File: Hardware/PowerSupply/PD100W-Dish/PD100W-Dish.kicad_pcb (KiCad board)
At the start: 4 copper layers, 66.8 x 66.2 mm, 164 parts

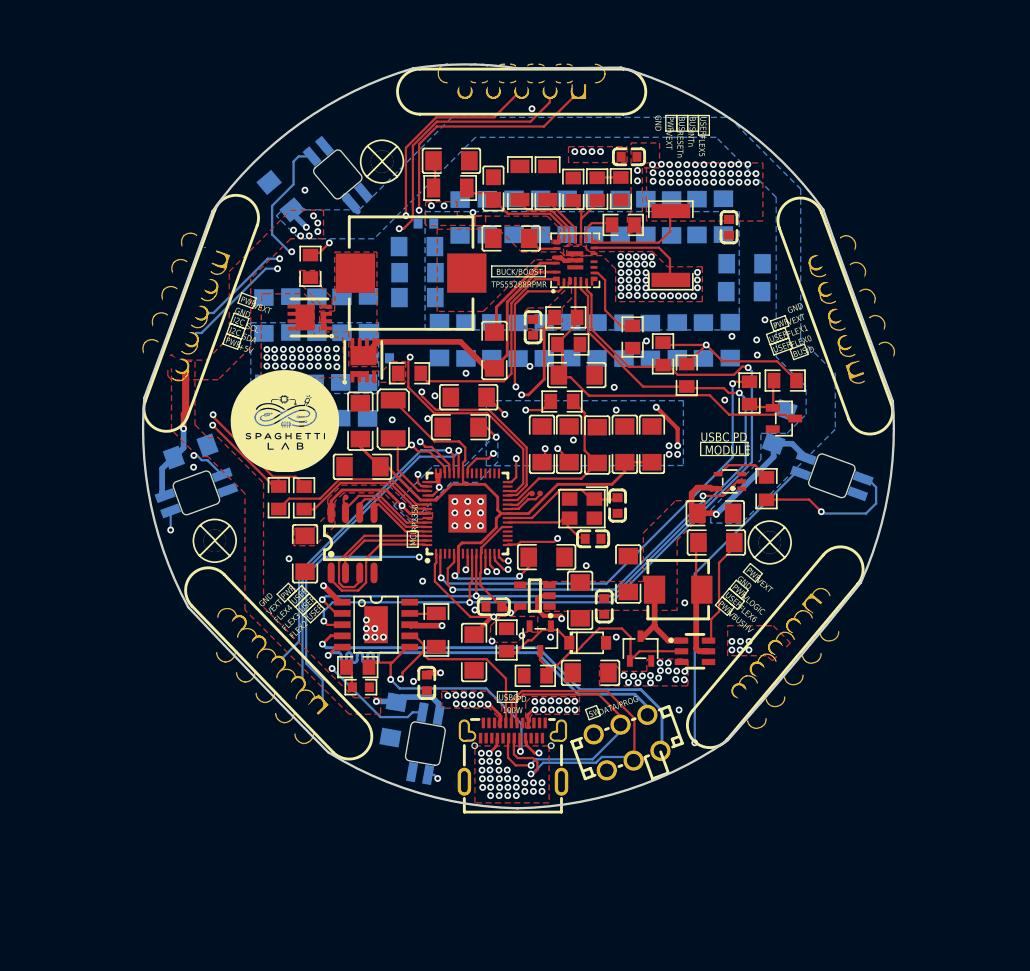
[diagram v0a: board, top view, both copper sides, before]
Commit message: Some minor fixes to silkscreen of all baords
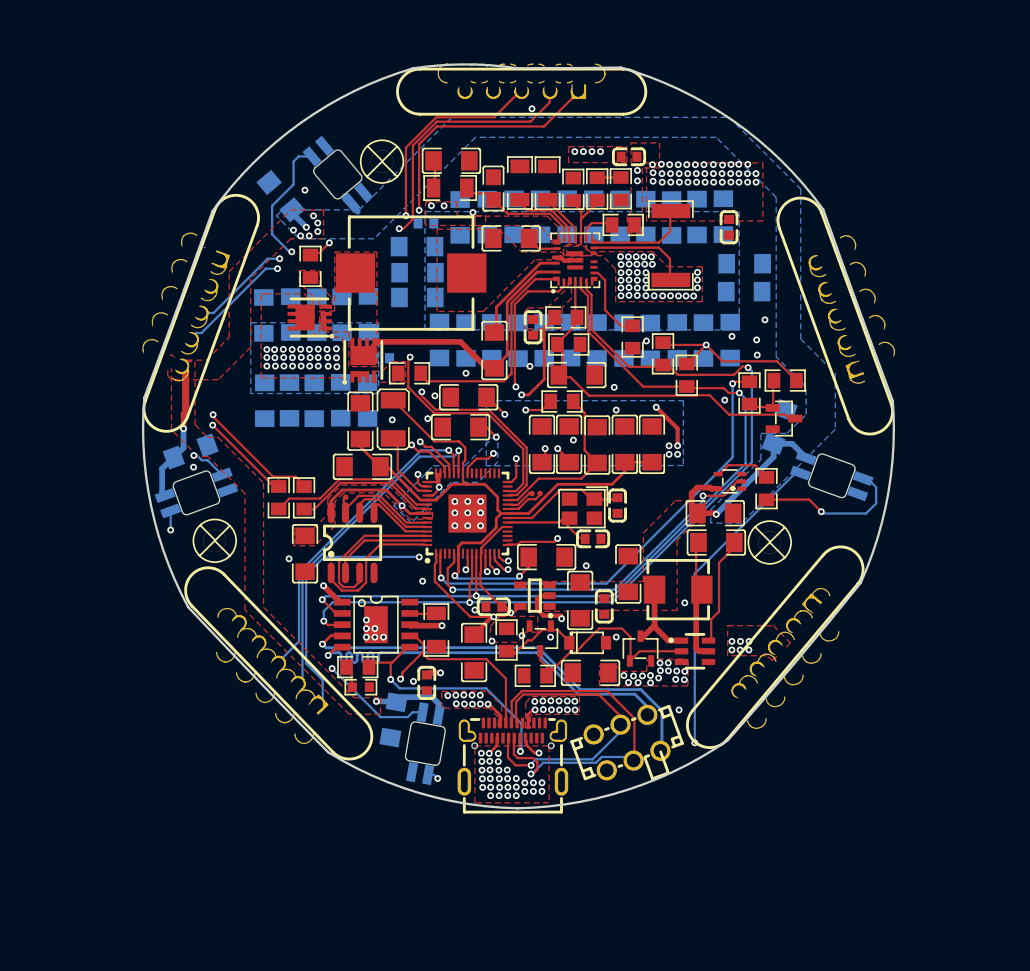
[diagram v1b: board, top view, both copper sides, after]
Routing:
- net VLOGIC: vias 19 -> 23
- net VHV: vias 62 -> 102
- net VEXT: vias 24 -> 38
- net VCC: vias 3 -> 4
- net IOSN+2: vias 23 -> 35
- net AGND: vias 118 -> 45
- net 5V: vias 8 -> 10
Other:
- board text added: "SCL_AUX"
- board text added: "SDA_AUX"
- board text added: "VHV"
- board text added: "~{INT}"
- board text added: "~{RESET}"
- board text removed: "100W"
- board text removed: "BUCK/BOOST"
- board text removed: "BUS"
- board text removed: "DATA/PROG"
- board text removed: "I2C"
- board text removed: "INTn"
- board text removed: "MCU"
- board text removed: "MODULE"
- board text removed: "PD"
- board text removed: "PWR"
- board text removed: "RESETn"
- board text removed: "RP2350"
- board text removed: "SCL"
- board text removed: "SDA"
- board text removed: "SW"
- board text removed: "TPS55288RPMR"
- board text removed: "USBC"
- board text removed: "USBC PD"
- board text removed: "USER"
- board text removed: "VBUSHV"

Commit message: Fixes to ratnest of PD100W ATTENTION: not a definitve layout, print at your own risk
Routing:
- net AGND: track 6.47 -> 17.8 mm, vias 45 -> 52
- net VCC: track 0.00 -> 5.42 mm
- net 5V: track 49.6 -> 53.1 mm
- net IOSN+2: track 9.00 -> 10.7 mm
- added copper zone on B.Cu, net AGND
- added copper zone on In1.Cu, net AGND
